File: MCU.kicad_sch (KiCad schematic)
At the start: 0 parts

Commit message: Progress commit. Added MCU + IMU.
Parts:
- added U2: STM32L432KCUx, Package_DFN_QFN:QFN-32-1EP_5x5mm_P0.5mm_EP3.45x3.45mm, symbol MCU_ST_STM32L4:STM32L432KCUx
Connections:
- new net: U2.16 (VSS), U2.32 (VSS), U2.33 (VSS)
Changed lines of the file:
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@@
 	(generator_version "8.0")
 	(paper "A4")
+	(symbol
+		(lib_id "MCU_ST_STM32L4:STM32L432KCUx")
+		(at 91.44 77.47 0)
+		(unit 1)
+		(exclude_from_sim no)
+		(in_bom yes)
+		(on_board yes)
+		(dnp no)
+		(fields_autoplaced yes)
+		(property "Reference" "U2"
+			(at 93.6341 102.87 0)
+			(effects
+				(font
+					(size 1.27 1.27)
+				)
+				(justify left)
+			)
+		)
+		(property "Value" "STM32L432KCUx"
+			(at 93.6341 105.41 0)
+			(effects
+				(font
+					(size 1.27 1.27)
+				)
+				(justify left)
+			)
+		)
+		(property "Footprint" "Package_DFN_QFN:QFN-32-1EP_5x5mm_P0.5mm_EP3.45x3.45mm"
+			(at 81.28 100.33 0)
+			(effects
+				(font
+					(size 1.27 1.27)
+				)
+				(justify right)
+				(hide yes)
+			)
+		)
+		(property "Datasheet" "https://www.st.com/resource/en/datasheet/stm32l432kc.pdf"
+			(at 91.44 77.47 0)
+			(effects
+				(font
+					(size 1.27 1.27)
+				)
+				(hide yes)
+			)
+		)
+		(property "Description" "STMicroelectronics Arm Cortex-M4 MCU, 256KB flash, 64KB RAM, 80 MHz, 1.71-3.6V, 26 GPIO, UFQFPN32"
+			(at 91.44 77.47 0)
+			(effects
+				(font
+					(size 1.27 1.27)
+				)
+				(hide yes)
+			)
+		)
+		(pin "14"
+		)
+		(pin "8"
+		)
+		(pin "33"
+		)
+		(pin "4"
+		)
+		(pin "21"
+		)
+		(pin "16"
+		)
+		(pin "12"
+		)
+		(pin "7"
+		)
+		(pin "13"
+		)
+		(pin "17"
+		)
+		(pin "18"
+		)
+		(pin "31"
+		)
+		(pin "9"
+		)
+		(pin "1"
+		)
+		(pin "19"
+		)
+		(pin "10"
+		)
+		(pin "5"
+		)
+		(pin "25"
+		)
+		(pin "26"
+		)
+		(pin "3"
+		)
+		(pin "28"
+		)
+		(pin "24"
+		)
+		(pin "27"
+		)
+		(pin "6"
+		)
+		(pin "2"
+		)
+		(pin "32"
+		)
+		(pin "30"
+		)
+		(pin "29"
+		)
+		(pin "22"
+		)
+		(pin "11"
+		)
+		(pin "20"
+		)
+		(pin "15"
+		)
+		(pin "23"
+		)
+		(instances
+			(project ""
+				(path "/a75630d2-15a7-42bc-8ce0-7846cbd1da6b/c8d454a4-a64d-492c-9043-c9910b58426e"
+					(reference "U2")
+					(unit 1)
+				)
+			)
+		)
+	)
 )

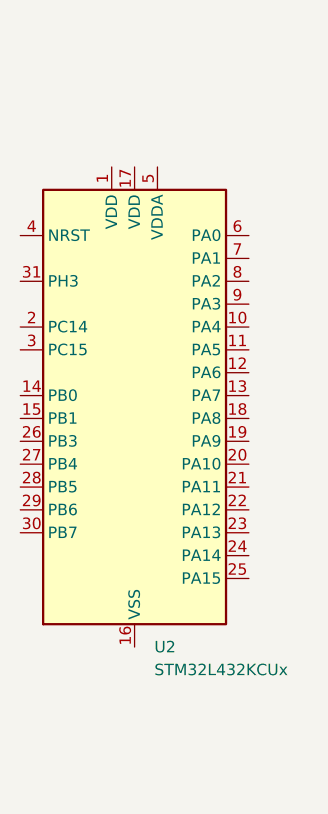
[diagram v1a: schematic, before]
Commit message: Finished power section.
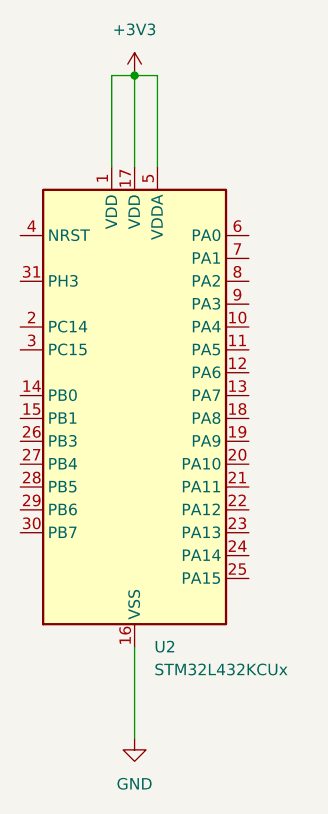
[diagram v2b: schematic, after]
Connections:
- net +3V3: now reaches U2.1 (VDD)
- net +3V3: now also U2.17 (VDD), U2.5 (VDDA)
- net GND: now reaches U2.16 (VSS), U2.32 (VSS), U2.33 (VSS)
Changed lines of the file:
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@@
 (kicad_sch
-	(version 20231120)
+	(version 20250114)
 	(generator "eeschema")
-	(generator_version "8.0")
+	(generator_version "9.0")
 	(paper "A4")
+	(junction
+		(at 91.44 39.37)
+		(diameter 0)
+		(color 0 0 0 0)
+	)
+	(wire
+		(pts
+			(xy 88.9 39.37) (xy 91.44 39.37)
+		)
+		(stroke
+			(width 0)
+			(type default)
+		)
+	)
+	(wire
+		(pts
+			(xy 88.9 49.53) (xy 88.9 39.37)
+		)
+		(stroke
+			(width 0)
+			(type default)
+		)
+	)
+	(wire
+		(pts
+			(xy 93.98 49.53) (xy 93.98 39.37)
+		)
+		(stroke
+			(width 0)
+			(type default)
+		)
+	)
+	(wire
+		(pts
+			(xy 93.98 39.37) (xy 91.44 39.37)
+		)
+		(stroke
+			(width 0)
+			(type default)
+		)
+	)
+	(wire
+		(pts
+			(xy 91.44 39.37) (xy 91.44 49.53)
+		)
+		(stroke
+			(width 0)
+			(type default)
+		)
+	)
+	(wire
+		(pts
+			(xy 91.44 102.87) (xy 91.44 113.03)
+		)
+		(stroke
+			(width 0)
+			(type default)
+		)
+	)
+	(symbol
+		(lib_id "power:GND")
+		(at 91.44 113.03 0)
+		(unit 1)
+		(exclude_from_sim no)
+		(in_bom yes)
+		(on_board yes)
+		(dnp no)
+		(fields_autoplaced yes)
+		(property "Reference" "#PWR9"
+			(at 91.44 119.38 0)
+			(effects
+				(font
+					(size 1.27 1.27)
+				)
+				(hide yes)
+			)
+		)
+		(property "Value" "GND"
+			(at 91.44 118.11 0)
+			(effects
+				(font
+					(size 1.27 1.27)
+				)
+			)
+		)
+		(property "Footprint" ""
+			(at 91.44 113.03 0)
+			(effects
+				(font
+					(size 1.27 1.27)
+				)
+				(hide yes)
+			)
+		)
+		(property "Datasheet" ""
+			(at 91.44 113.03 0)
+			(effects
+				(font
+					(size 1.27 1.27)
+				)
+				(hide yes)
+			)
+		)
+		(property "Description" "Power symbol creates a global label with name \"GND\" , ground"
+			(at 91.44 113.03 0)
+			(effects
+				(font
+					(size 1.27 1.27)
+				)
+				(hide yes)
+			)
+		)
+		(pin "1"
+		)
+		(instances
+			(project ""
+				(path "/a75630d2-15a7-42bc-8ce0-7846cbd1da6b/c8d454a4-a64d-492c-9043-c9910b58426e"
+					(reference "#PWR9")
+					(unit 1)
+				)
+			)
+		)
+	)
 	(symbol
 		(lib_id "MCU_ST_STM32L4:STM32L432KCUx")
@@
 					(unit 1)
 				)
+			)
+		)
+	)
+	(symbol
+		(lib_id "power:+3V3")
+		(at 91.44 39.37 0)
+		(unit 1)
+		(exclude_from_sim no)
+		(in_bom yes)
+		(on_board yes)
+		(dnp no)
+		(fields_autoplaced yes)
+		(property "Reference" "#PWR8"
+			(at 91.44 43.18 0)
+			(effects
+				(font
+					(size 1.27 1.27)
+				)
+				(hide yes)
+			)
+		)
+		(property "Value" "+3V3"
+			(at 91.44 34.29 0)
+			(effects
+				(font
+					(size 1.27 1.27)
+				)
+			)
+		)
+		(property "Footprint" ""
+			(at 91.44 39.37 0)
+			(effects
+				(font
+					(size 1.27 1.27)
+				)
+				(hide yes)
+			)
+		)
+		(property "Datasheet" ""
+			(at 91.44 39.37 0)
+			(effects
+				(font
+					(size 1.27 1.27)
+				)
+				(hide yes)
+			)
+		)
+		(property "Description" "Power symbol creates a global label with name \"+3V3\""
+			(at 91.44 39.37 0)
+			(effects
+				(font
+					(size 1.27 1.27)
+				)
+				(hide yes)
+			)
+		)
+		(pin "1"
+		)
+		(instances
+			(project ""
+				(path "/a75630d2-15a7-42bc-8ce0-7846cbd1da6b/c8d454a4-a64d-492c-9043-c9910b58426e"
+					(reference "#PWR8")
+					(unit 1)
+				)

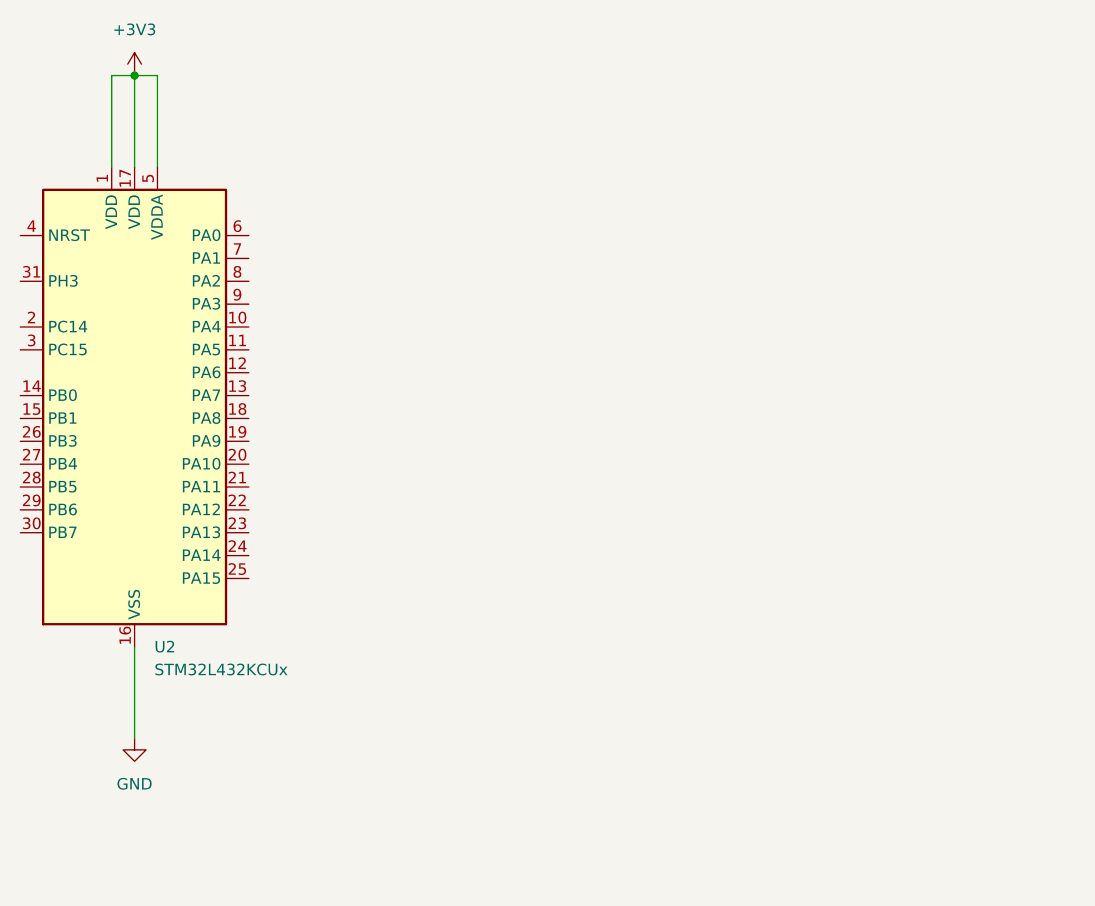
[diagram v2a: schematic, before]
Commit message: Finished LSM6DSOX schematic
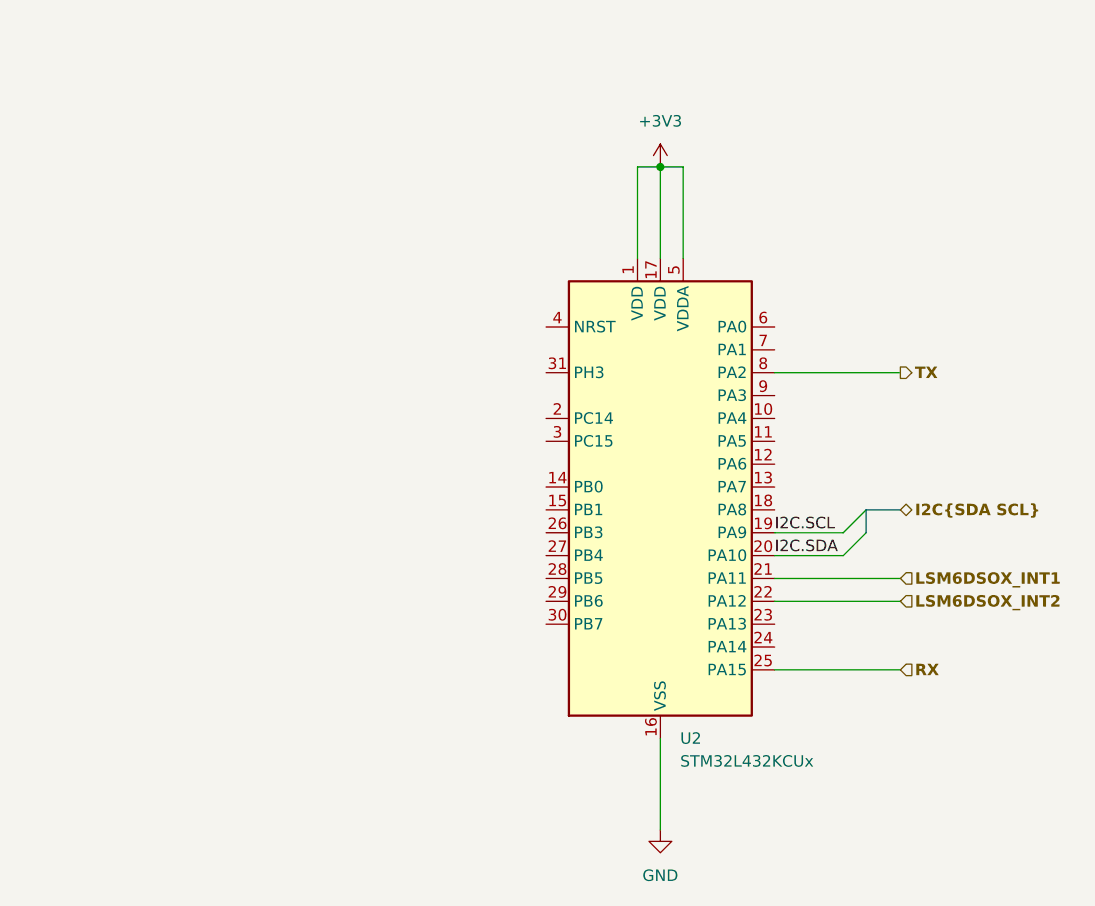
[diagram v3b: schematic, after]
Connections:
- net I2C.SCL: now reaches U2.19 (PA9)
- net I2C.SDA: now reaches U2.20 (PA10)
- net LSM6DSOX_INT1: now reaches U2.21 (PA11)
- net LSM6DSOX_INT2: now reaches U2.22 (PA12)
- net RX: now reaches U2.25 (PA15)
- net TX: now reaches U2.8 (PA2)
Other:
- moved on the sheet: U2
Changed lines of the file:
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@@
 	(paper "A4")
 	(junction
-		(at 91.44 39.37)
+		(at 149.86 49.53)
 		(diameter 0)
 		(color 0 0 0 0)
 	)
-	(wire
-		(pts
-			(xy 88.9 39.37) (xy 91.44 39.37)
-		)
-		(stroke
-			(width 0)
-			(type default)
-		)
-	)
-	(wire
-		(pts
-			(xy 88.9 49.53) (xy 88.9 39.37)
-		)
-		(stroke
-			(width 0)
-			(type default)
-		)
-	)
-	(wire
-		(pts
-			(xy 93.98 49.53) (xy 93.98 39.37)
-		)
-		(stroke
-			(width 0)
-			(type default)
-		)
-	)
-	(wire
-		(pts
-			(xy 93.98 39.37) (xy 91.44 39.37)
-		)
-		(stroke
-			(width 0)
-			(type default)
-		)
-	)
-	(wire
-		(pts
-			(xy 91.44 39.37) (xy 91.44 49.53)
-		)
-		(stroke
-			(width 0)
-			(type default)
-		)
-	)
-	(wire
-		(pts
-			(xy 91.44 102.87) (xy 91.44 113.03)
-		)
-		(stroke
-			(width 0)
-			(type default)
+	(bus_entry
+		(at 172.72 90.17)
+		(size -2.54 2.54)
+		(stroke
+			(width 0)
+			(type default)
+		)
+	)
+	(bus_entry
+		(at 172.72 87.63)
+		(size -2.54 2.54)
+		(stroke
+			(width 0)
+			(type default)
+		)
+	)
+	(wire
+		(pts
+			(xy 176.53 97.79) (xy 162.56 97.79)
+		)
+		(stroke
+			(width 0)
+			(type default)
+		)
+	)
+	(wire
+		(pts
+			(xy 147.32 49.53) (xy 149.86 49.53)
+		)
+		(stroke
+			(width 0)
+			(type default)
+		)
+	)
+	(wire
+		(pts
+			(xy 162.56 95.25) (xy 176.53 95.25)
+		)
+		(stroke
+			(width 0)
+			(type default)
+		)
+	)
+	(wire
+		(pts
+			(xy 147.32 59.69) (xy 147.32 49.53)
+		)
+		(stroke
+			(width 0)
+			(type default)
+		)
+	)
+	(wire
+		(pts
+			(xy 152.4 59.69) (xy 152.4 49.53)
+		)
+		(stroke
+			(width 0)
+			(type default)
+		)
+	)
+	(wire
+		(pts
+			(xy 152.4 49.53) (xy 149.86 49.53)
+		)
+		(stroke
+			(width 0)
+			(type default)
+		)
+	)
+	(wire
+		(pts
+			(xy 170.18 90.17) (xy 162.56 90.17)
+		)
+		(stroke
+			(width 0)
+			(type default)
+		)
+	)
+	(wire
+		(pts
+			(xy 162.56 105.41) (xy 176.53 105.41)
+		)
+		(stroke
+			(width 0)
+			(type default)
+		)
+	)
+	(bus
+		(pts
+			(xy 172.72 87.63) (xy 176.53 87.63)
+		)
+		(stroke
+			(width 0)
+			(type default)
+		)
+	)
+	(wire
+		(pts
+			(xy 162.56 92.71) (xy 170.18 92.71)
+		)
+		(stroke
+			(width 0)
+			(type default)
+		)
+	)
+	(wire
+		(pts
+			(xy 149.86 49.53) (xy 149.86 59.69)
+		)
+		(stroke
+			(width 0)
+			(type default)
+		)
+	)
+	(wire
+		(pts
+			(xy 149.86 113.03) (xy 149.86 123.19)
+		)
+		(stroke
+			(width 0)
+			(type default)
+		)
+	)
+	(wire
+		(pts
+			(xy 162.56 72.39) (xy 176.53 72.39)
+		)
+		(stroke
+			(width 0)
+			(type default)
+		)
+	)
+	(bus
+		(pts
+			(xy 172.72 87.63) (xy 172.72 90.17)
+		)
+		(stroke
+			(width 0)
+			(type default)
+		)
+	)
+	(label "I2C.SDA"
+		(at 162.56 92.71 0)
+		(effects
+			(font
+				(size 1.27 1.27)
+			)
+			(justify left bottom)
+		)
+	)
+	(label "I2C.SCL"
+		(at 162.56 90.17 0)
+		(effects
+			(font
+				(size 1.27 1.27)
+			)
+			(justify left bottom)
+		)
+	)
+	(hierarchical_label "RX"
+		(shape input)
+		(at 176.53 105.41 0)
+		(effects
+			(font
+				(size 1.27 1.27)
+				(thickness 0.254)
+				(bold yes)
+			)
+			(justify left)
+		)
+	)
+	(hierarchical_label "TX"
+		(shape output)
+		(at 176.53 72.39 0)
+		(effects
+			(font
+				(size 1.27 1.27)
+				(thickness 0.254)
+				(bold yes)
+			)
+			(justify left)
+		)
+	)
+	(hierarchical_label "I2C{SDA SCL}"
+		(shape bidirectional)
+		(at 176.53 87.63 0)
+		(effects
+			(font
+				(size 1.27 1.27)
+				(thickness 0.254)
+				(bold yes)
+			)
+			(justify left)
+		)
+	)
+	(hierarchical_label "LSM6DSOX_INT1"
+		(shape input)
+		(at 176.53 95.25 0)
+		(effects
+			(font
+				(size 1.27 1.27)
+				(thickness 0.254)
+				(bold yes)
+			)
+			(justify left)
+		)
+	)
+	(hierarchical_label "LSM6DSOX_INT2"
+		(shape input)
+		(at 176.53 97.79 0)
+		(effects
+			(font
+				(size 1.27 1.27)
+				(thickness 0.254)
+				(bold yes)
+			)
+			(justify left)
 		)
 	)
 	(symbol
 		(lib_id "power:GND")
-		(at 91.44 113.03 0)
+		(at 149.86 123.19 0)
 		(unit 1)
 		(exclude_from_sim no)
@@
 		(fields_autoplaced yes)
 		(property "Reference" "#PWR9"
-			(at 91.44 119.38 0)
+			(at 149.86 129.54 0)
 			(effects
 				(font
@@
 		)
 		(property "Value" "GND"
-			(at 91.44 118.11 0)
+			(at 149.86 128.27 0)
 			(effects
 				(font
@@
 		)
 		(property "Footprint" ""
-			(at 91.44 113.03 0)
+			(at 149.86 123.19 0)
 			(effects
 				(font
@@
 		)
 		(property "Datasheet" ""
-			(at 91.44 113.03 0)
+			(at 149.86 123.19 0)
 			(effects
 				(font
@@
 		)
 		(property "Description" "Power symbol creates a global label with name \"GND\" , ground"
-			(at 91.44 113.03 0)
+			(at 149.86 123.19 0)
 			(effects
 				(font
@@
 	(symbol
 		(lib_id "MCU_ST_STM32L4:STM32L432KCUx")
-		(at 91.44 77.47 0)
+		(at 149.86 87.63 0)
 		(unit 1)
 		(exclude_from_sim no)
@@
 		(fields_autoplaced yes)
 		(property "Reference" "U2"
-			(at 93.6341 102.87 0)
+			(at 152.0541 113.03 0)
 			(effects
 				(font
@@
 		)
 		(property "Value" "STM32L432KCUx"
-			(at 93.6341 105.41 0)
+			(at 152.0541 115.57 0)
 			(effects
 				(font
@@
 		)
 		(property "Footprint" "Package_DFN_QFN:QFN-32-1EP_5x5mm_P0.5mm_EP3.45x3.45mm"
-			(at 81.28 100.33 0)
+			(at 139.7 110.49 0)
 			(effects
 				(font
@@
 		)
 		(property "Datasheet" "https://www.st.com/resource/en/datasheet/stm32l432kc.pdf"
-			(at 91.44 77.47 0)
+			(at 149.86 87.63 0)
 			(effects
 				(font
@@
 		)
 		(property "Description" "STMicroelectronics Arm Cortex-M4 MCU, 256KB flash, 64KB RAM, 80 MHz, 1.71-3.6V, 26 GPIO, UFQFPN32"
-			(at 91.44 77.47 0)
+			(at 149.86 87.63 0)
 			(effects
 				(font
@@
 	(symbol
 		(lib_id "power:+3V3")
-		(at 91.44 39.37 0)
+		(at 149.86 49.53 0)
 		(unit 1)
 		(exclude_from_sim no)
@@
 		(fields_autoplaced yes)
 		(property "Reference" "#PWR8"
-			(at 91.44 43.18 0)
+			(at 149.86 53.34 0)
 			(effects
 				(font
@@
 		)
 		(property "Value" "+3V3"
-			(at 91.44 34.29 0)
+			(at 149.86 44.45 0)
 			(effects
 				(font
@@
 		)
 		(property "Footprint" ""
-			(at 91.44 39.37 0)
+			(at 149.86 49.53 0)
 			(effects
 				(font
@@
 		)
 		(property "Datasheet" ""
-			(at 91.44 39.37 0)
+			(at 149.86 49.53 0)
 			(effects
 				(font
@@
 		)
 		(property "Description" "Power symbol creates a global label with name \"+3V3\""
-			(at 91.44 39.37 0)
-			(effects
-				(font
+			(at 149.86 49.53 0)
+			(effects
+				(font

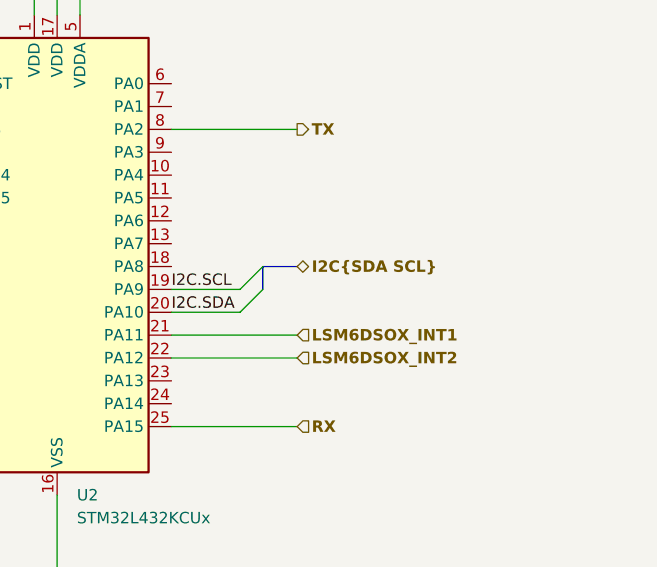
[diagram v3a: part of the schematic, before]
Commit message: Initial complete implementation of LEDS.
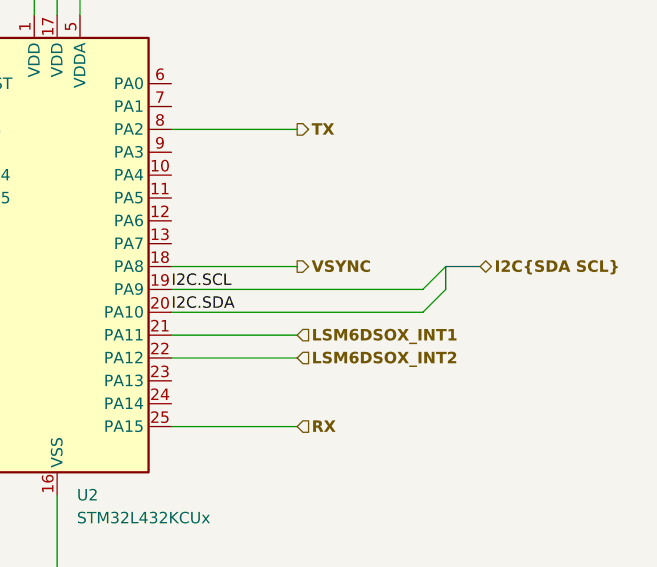
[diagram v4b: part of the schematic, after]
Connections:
- net VSYNC: now reaches U2.18 (PA8)
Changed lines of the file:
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@@
 	)
 	(bus_entry
-		(at 172.72 90.17)
+		(at 193.04 90.17)
 		(size -2.54 2.54)
 		(stroke
@@
 	)
 	(bus_entry
-		(at 172.72 87.63)
+		(at 193.04 87.63)
 		(size -2.54 2.54)
 		(stroke
@@
 	(wire
 		(pts
-			(xy 170.18 90.17) (xy 162.56 90.17)
+			(xy 190.5 90.17) (xy 162.56 90.17)
 		)
 		(stroke
@@
 	(bus
 		(pts
-			(xy 172.72 87.63) (xy 176.53 87.63)
-		)
-		(stroke
-			(width 0)
-			(type default)
-		)
-	)
-	(wire
-		(pts
-			(xy 162.56 92.71) (xy 170.18 92.71)
+			(xy 193.04 87.63) (xy 196.85 87.63)
+		)
+		(stroke
+			(width 0)
+			(type default)
+		)
+	)
+	(wire
+		(pts
+			(xy 162.56 87.63) (xy 176.53 87.63)
+		)
+		(stroke
+			(width 0)
+			(type default)
+		)
+	)
+	(wire
+		(pts
+			(xy 162.56 92.71) (xy 190.5 92.71)
 		)
 		(stroke
@@
 	(bus
 		(pts
-			(xy 172.72 87.63) (xy 172.72 90.17)
+			(xy 193.04 87.63) (xy 193.04 90.17)
 		)
 		(stroke
@@
 	(hierarchical_label "I2C{SDA SCL}"
 		(shape bidirectional)
-		(at 176.53 87.63 0)
+		(at 196.85 87.63 0)
 		(effects
 			(font
@@
 		(effects
 			(font
+				(size 1.27 1.27)
+				(thickness 0.254)
+				(bold yes)
+			)
+			(justify left)
+		)
+	)
+	(hierarchical_label "VSYNC"
+		(shape output)
+		(at 176.53 87.63 0)
+		(effects
+			(font
